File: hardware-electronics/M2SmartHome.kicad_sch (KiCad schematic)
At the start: 5 parts, among them J1 USB1055-GF-L-A_REVC3, J2 Micro_SD_Card_Det_Hirose_DM3AT, M1 M.2-B-KEY-2280-ADAPTER, U1 EMMC08G-ML36-01B00, U2 PI7C9X440SLBFDE

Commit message: Added created components to the PCB and draw 2280 outline
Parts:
- removed J1: USB1055-GF-L-A_REVC3, footprints:GCT_USB1055-GF-L-A_REVC3, symbol M2SmartHome:USB1055-GF-L-A_REVC3
- removed U1: EMMC08G-ML36-01B00, footprints:BGA153N50P14X14_1300X1150X100N, symbol M2SmartHome:EMMC08G-ML36-01B00
- removed U2: PI7C9X440SLBFDE, footprints:QFP40P1600X1600X160-129N, symbol M2SmartHome:PI7C9X440SLBFDE
- added U2: USB2244-AEZG-06, M2SmartHomeFootprints:USB2244-AEZG-06, symbol M2SmartHomeSymbols:USB2244-AEZG-06
- added U3: PI7C9X440SLBFDE, M2SmartHomeFootprints:PI7C9X440SLBFDE, symbol M2SmartHomeSymbols:PI7C9X440SLBFDE
- added U4, U5: CP2102N-A02-GQFN20, M2SmartHomeFootprints:CP2102N-A02-GQFN20, symbol M2SmartHomeSymbols:CP2102N-A02-GQFN20
- added U6: EFR32ZG14P231F256GM32-BR, M2SmartHomeFootprints:EFR32ZG14P231F256GM32-BR, symbol M2SmartHomeSymbols:EFR32ZG14P231F256GM32-BR
- added U9: EMMC16G-MW28-01E10, M2SmartHomeFootprints:EMMC16G-MW28-01E10, symbol M2SmartHomeSymbols:EMMC16G-MW28-01E10
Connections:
- new net: U3.100 (VDDC), U3.109 (VDDC), U3.111 (VDDC), U3.22 (VDDC), U3.35 (VDDC), U3.81 (VDDC)
- new net: U3.101 (VSS), U3.106 (VSS), U3.110 (VSS), U3.118 (VSS), U3.120 (VSS), U3.125 (VSS), U3.127 (VSS), U3.129 (VSS), U3.23 (VSS), U3.34 (VSS), U3.36 (VSS), U3.39 (VSS), U3.45 (VSS), U3.50 (VSS), U3.53 (VSS), U3.61 (VSS), U3.68 (VSS), U3.82 (VSS), U3.86 (VSS), U3.89 (VSS), U3.9 (VSS), U3.94 (VSS), U3.96 (VSS)
- new net: U3.105 (VDDR), U3.112 (VDDR), U3.33 (VDDR), U3.67 (VDDR), U3.8 (VDDR)
- new net: U3.115 (VDDA), U3.121 (VDDA), U3.122 (VDDA), U3.128 (VDDA), U3.83 (VDDA), U3.90 (VDDA), U3.91 (VDDA), U3.97 (VDDA)
- new net: U3.40 (AVDD), U3.46 (AVDD), U3.49 (AVDD), U3.60 (AVDD)
- new net: U4.12 (GND), U4.3 (GND), U4.EXP (GND)
- new net: U5.12 (GND), U5.3 (GND), U5.EXP (GND)
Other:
- moved on the sheet: J2, M1

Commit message: SCH basic division
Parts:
- removed J2: Micro_SD_Card_Det_Hirose_DM3AT, symbol Connector:Micro_SD_Card_Det_Hirose_DM3AT
- removed M1: M.2-B-KEY-2280-ADAPTER, footprints:M.2-B-KEY-2280-ADAPTER, symbol M2SmartHome:M.2-B-KEY-2280-ADAPTER
- removed U2: USB2244-AEZG-06, M2SmartHomeFootprints:USB2244-AEZG-06, symbol M2SmartHomeSymbols:USB2244-AEZG-06
- removed U4, U5: CP2102N-A02-GQFN20, M2SmartHomeFootprints:CP2102N-A02-GQFN20, symbol M2SmartHomeSymbols:CP2102N-A02-GQFN20
- removed U6: EFR32ZG14P231F256GM32-BR, M2SmartHomeFootprints:EFR32ZG14P231F256GM32-BR, symbol M2SmartHomeSymbols:EFR32ZG14P231F256GM32-BR
- removed U9: EMMC16G-MW28-01E10, M2SmartHomeFootprints:EMMC16G-MW28-01E10, symbol M2SmartHomeSymbols:EMMC16G-MW28-01E10
- added J1: M.2-Key-M-edge-connector, M2SmartHomeFootprints:M.2-Key-M-edge-connector, symbol M2SmartHomeSymbols:M.2-Key-M-edge-connector
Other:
- added sheet emmc (emmc.kicad_sch)
- added sheet sd-card (sd-card.kicad_sch)
- added sheet thread-or-zigbee (thread-or-zigbee.kicad_sch)
- added sheet z-wave (z-wave.kicad_sch)
- moved on the sheet: U3

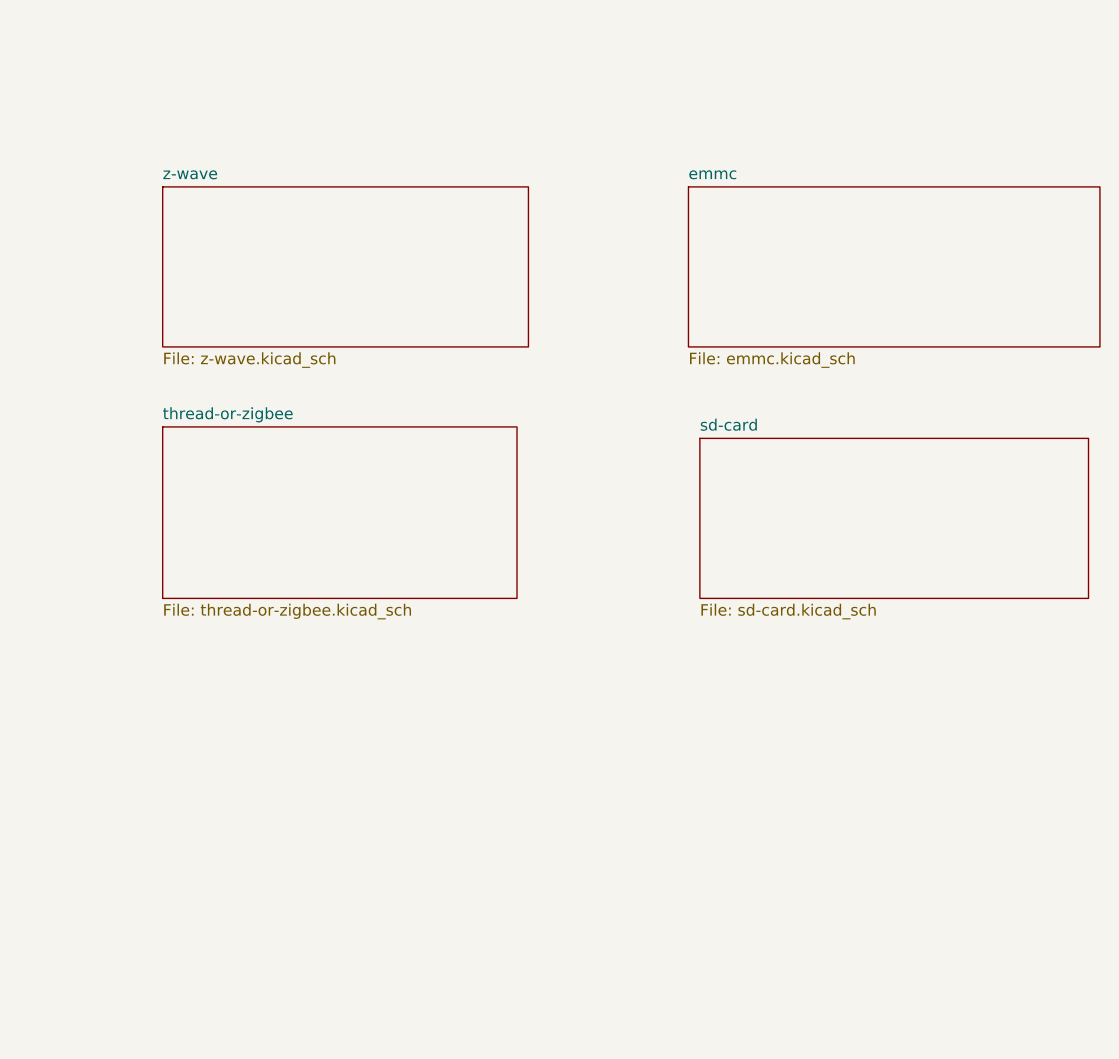
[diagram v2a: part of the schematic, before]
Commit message: SCH add block diagram #7
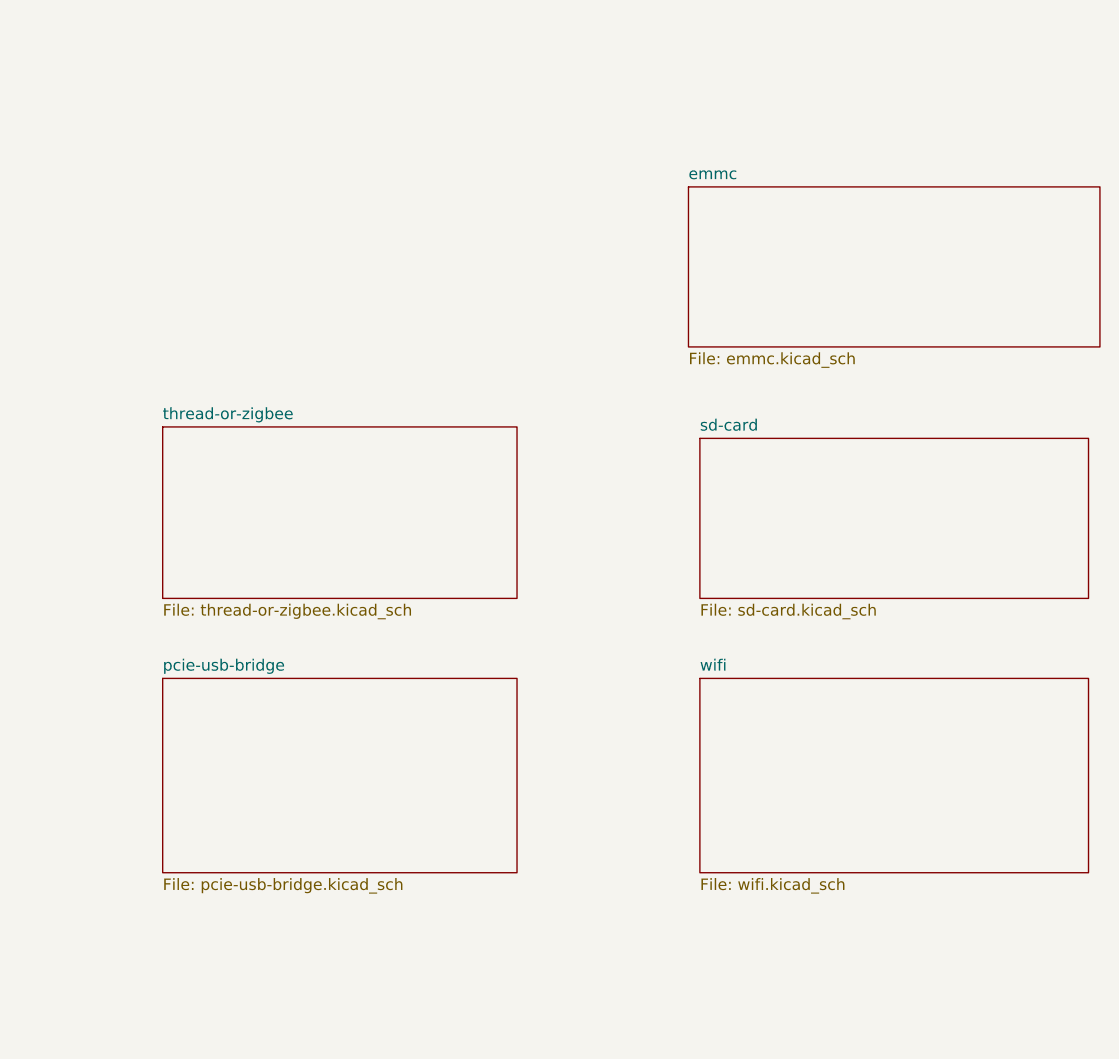
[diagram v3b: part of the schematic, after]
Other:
- removed sheet z-wave
- added sheet pcie-usb-bridge (pcie-usb-bridge.kicad_sch)
- added sheet wifi (wifi.kicad_sch)

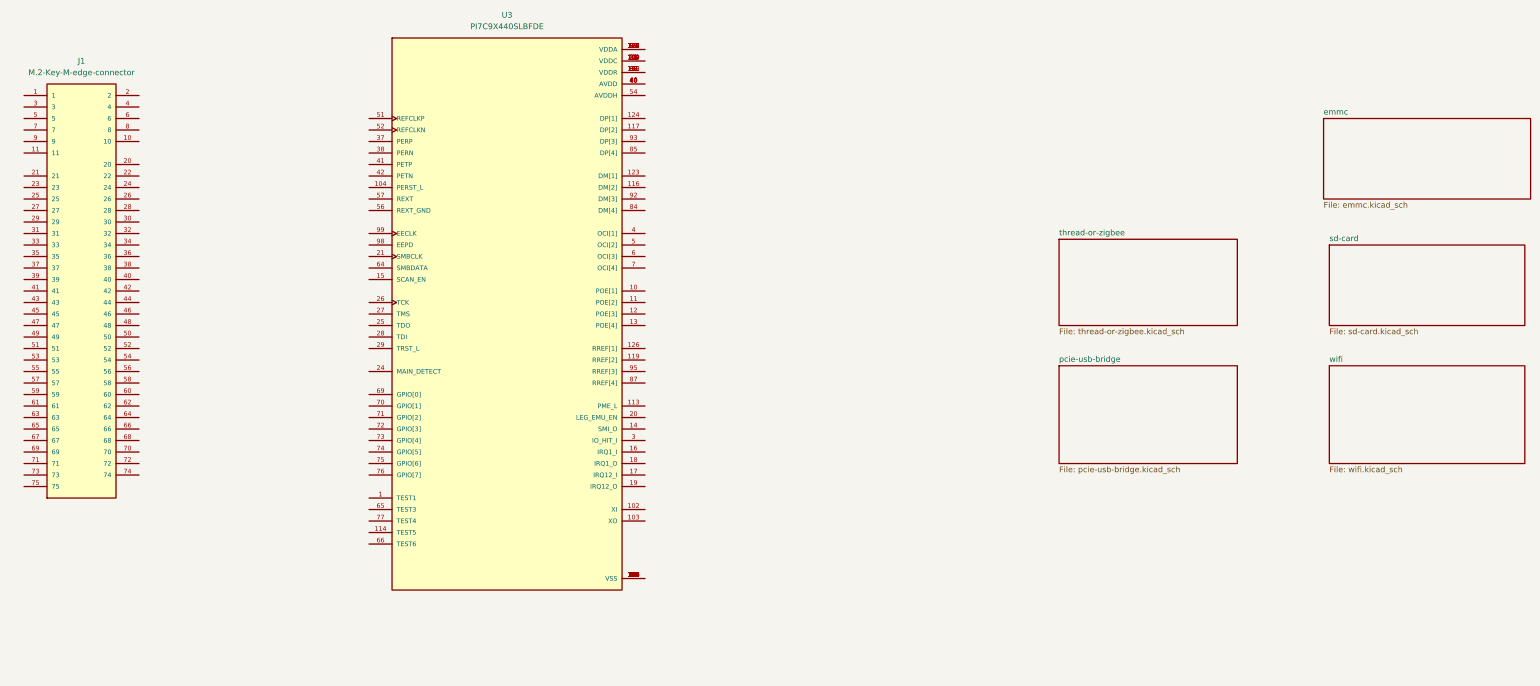
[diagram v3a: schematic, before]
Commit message: SCH organise schematic #7
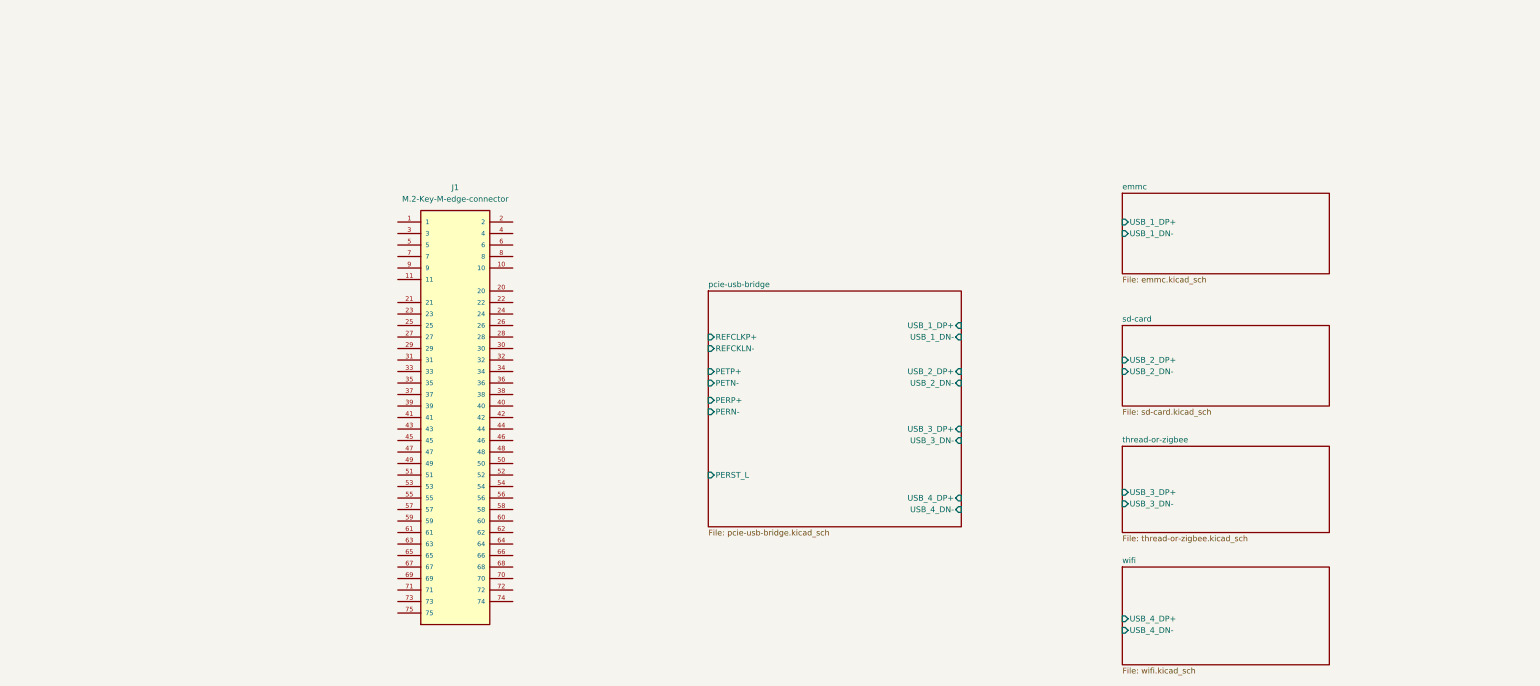
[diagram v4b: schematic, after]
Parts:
- removed U3: PI7C9X440SLBFDE, M2SmartHomeFootprints:PI7C9X440SLBFDE, symbol M2SmartHomeSymbols:PI7C9X440SLBFDE
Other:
- sheet emmc ports: added USB_1_DN-, USB_1_DP+; removed none
- sheet pcie-usb-bridge ports: added PERN-, PERP+, PERST_L, PETN-, PETP+, REFCKLN-, REFCLKP+, USB_1_DN-, USB_1_DP+, USB_2_DN-, USB_2_DP+, USB_3_DN-, USB_3_DP+, USB_4_DN-, USB_4_DP+; removed none
- sheet sd-card ports: added USB_2_DN-, USB_2_DP+; removed none
- sheet thread-or-zigbee ports: added USB_3_DN-, USB_3_DP+; removed none
- sheet wifi ports: added USB_4_DN-, USB_4_DP+; removed none
- moved on the sheet: J1

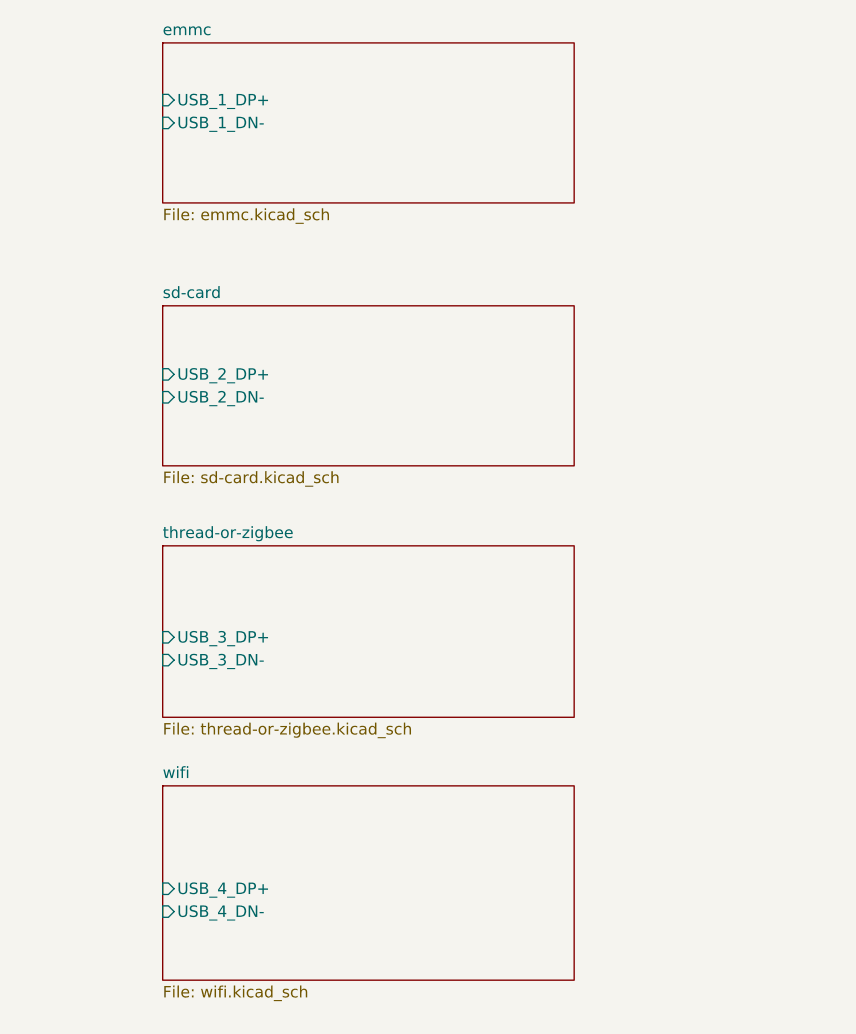
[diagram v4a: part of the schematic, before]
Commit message: [#8] SCH PCIe to USB replaced resistors
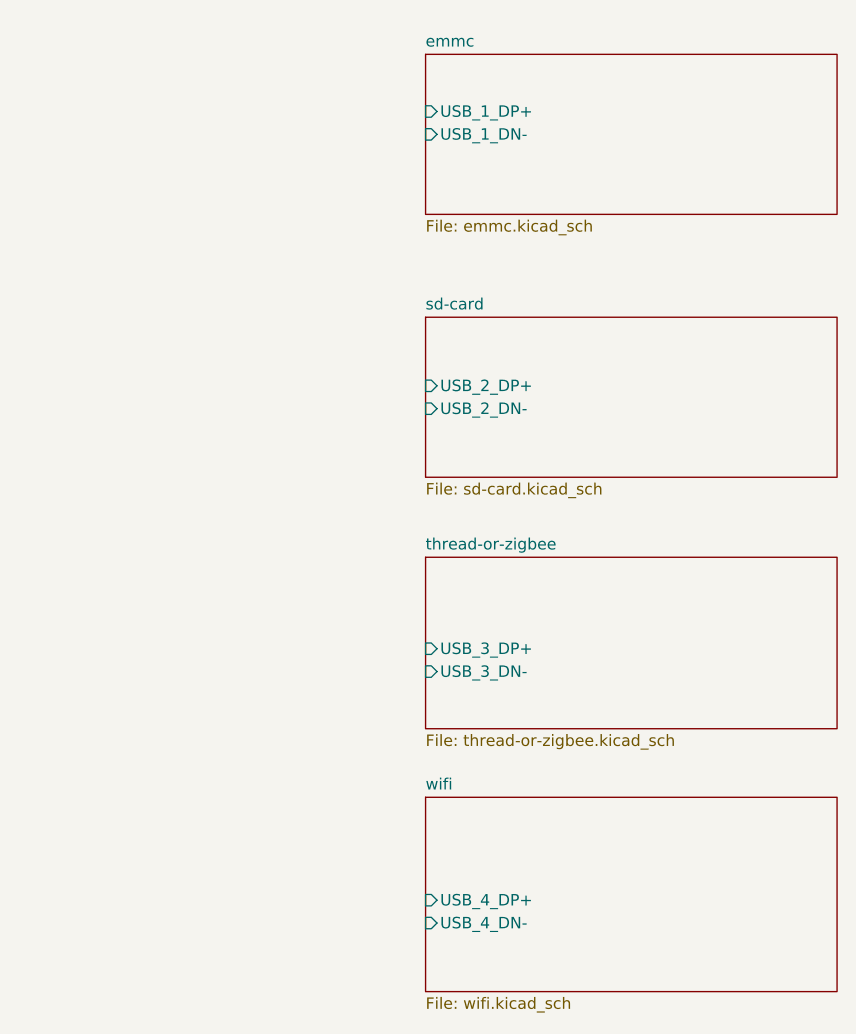
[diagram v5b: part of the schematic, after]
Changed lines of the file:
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@@
 	)
 	(sheet
-		(at 274.32 88.9)
+		(at 303.53 90.17)
 		(size 45.72 17.78)
 		(fields_autoplaced yes)
@@
 		)
 		(property "Sheetname" "sd-card"
-			(at 274.32 88.1884 0)
+			(at 303.53 89.4584 0)
 			(effects
 				(font
@@
 		)
 		(property "Sheetfile" "sd-card.kicad_sch"
-			(at 274.32 107.2646 0)
+			(at 303.53 108.5346 0)
 			(effects
 				(font
@@
 		)
 		(pin "USB_2_DN-" input
-			(at 274.32 99.06 180)
+			(at 303.53 100.33 180)
 			(effects
 				(font
@@
 		)
 		(pin "USB_2_DP+" input
-			(at 274.32 96.52 180)
+			(at 303.53 97.79 180)
 			(effects
 				(font
@@
 	)
 	(sheet
-		(at 274.32 142.24)
+		(at 303.53 143.51)
 		(size 45.72 21.59)
 		(fields_autoplaced yes)
@@
 		)
 		(property "Sheetname" "wifi"
-			(at 274.32 141.5284 0)
+			(at 303.53 142.7984 0)
 			(effects
 				(font
@@
 		)
 		(property "Sheetfile" "wifi.kicad_sch"
-			(at 274.32 164.4146 0)
+			(at 303.53 165.6846 0)
 			(effects
 				(font
@@
 		)
 		(pin "USB_4_DN-" input
-			(at 274.32 156.21 180)
+			(at 303.53 157.48 180)
 			(effects
 				(font
@@
 		)
 		(pin "USB_4_DP+" input
-			(at 274.32 153.67 180)
+			(at 303.53 154.94 180)
 			(effects
 				(font
@@
 	)
 	(sheet
-		(at 274.32 115.57)
+		(at 303.53 116.84)
 		(size 45.72 19.05)
 		(fields_autoplaced yes)
@@
 		)
 		(property "Sheetname" "thread-or-zigbee"
-			(at 274.32 114.8584 0)
+			(at 303.53 116.1284 0)
 			(effects
 				(font
@@
 		)
 		(property "Sheetfile" "thread-or-zigbee.kicad_sch"
-			(at 274.32 135.2046 0)
+			(at 303.53 136.4746 0)
 			(effects
 				(font
@@
 		)
 		(pin "USB_3_DN-" input
-			(at 274.32 128.27 180)
+			(at 303.53 129.54 180)
 			(effects
 				(font
@@
 		)
 		(pin "USB_3_DP+" input
-			(at 274.32 125.73 180)
+			(at 303.53 127 180)
 			(effects
 				(font
@@
 	)
 	(sheet
-		(at 274.32 59.69)
+		(at 303.53 60.96)
 		(size 45.72 17.78)
 		(fields_autoplaced yes)
@@
 		)
 		(property "Sheetname" "emmc"
-			(at 274.32 58.9784 0)
+			(at 303.53 60.2484 0)
 			(effects
 				(font
@@
 		)
 		(property "Sheetfile" "emmc.kicad_sch"
-			(at 274.32 78.0546 0)
+			(at 303.53 79.3246 0)
 			(effects
 				(font
@@
 		)
 		(pin "USB_1_DP+" input
-			(at 274.32 66.04 180)
+			(at 303.53 67.31 180)
 			(effects
 				(font
@@
 		)
 		(pin "USB_1_DN-" input
-			(at 274.32 68.58 180)
-			(effects
-				(font
+			(at 303.53 69.85 180)
+			(effects
+				(font
